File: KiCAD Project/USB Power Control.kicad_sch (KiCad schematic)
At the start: 24 parts, among them U5 TPS2561DRCR, U6 TPS2561DRCR, Y1 ECS-2520MV-240-BL-TR

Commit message: v1.0.0 RC2
Build candidate 2
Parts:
- U5, U6: Spec (none) -> TPS2561DRCR
- Y1: Spec (none) -> ECS-2520MV-240-BL-TR
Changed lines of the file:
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@@
 			)
 		)
+		(property "Spec" "TPS2561DRCR"
+			(at 96.52 27.94 0)
+			(effects
+				(font
+					(size 1.27 1.27)
+				)
+			)
+		)
 		(pin "10"
 		)
@@
 			)
 		)
+		(property "Spec" "TPS2561DRCR"
+			(at 96.52 91.44 0)
+			(effects
+				(font
+					(size 1.27 1.27)
+				)
+			)
+		)
 		(pin "10"
 		)
@@
 			)
 		)
+		(property "Spec" "ECS-2520MV-240-BL-TR"
+			(at 96.52 154.94 0)
+			(effects
+				(font
+					(size 1.27 1.27)
+				)
+			)
+		)

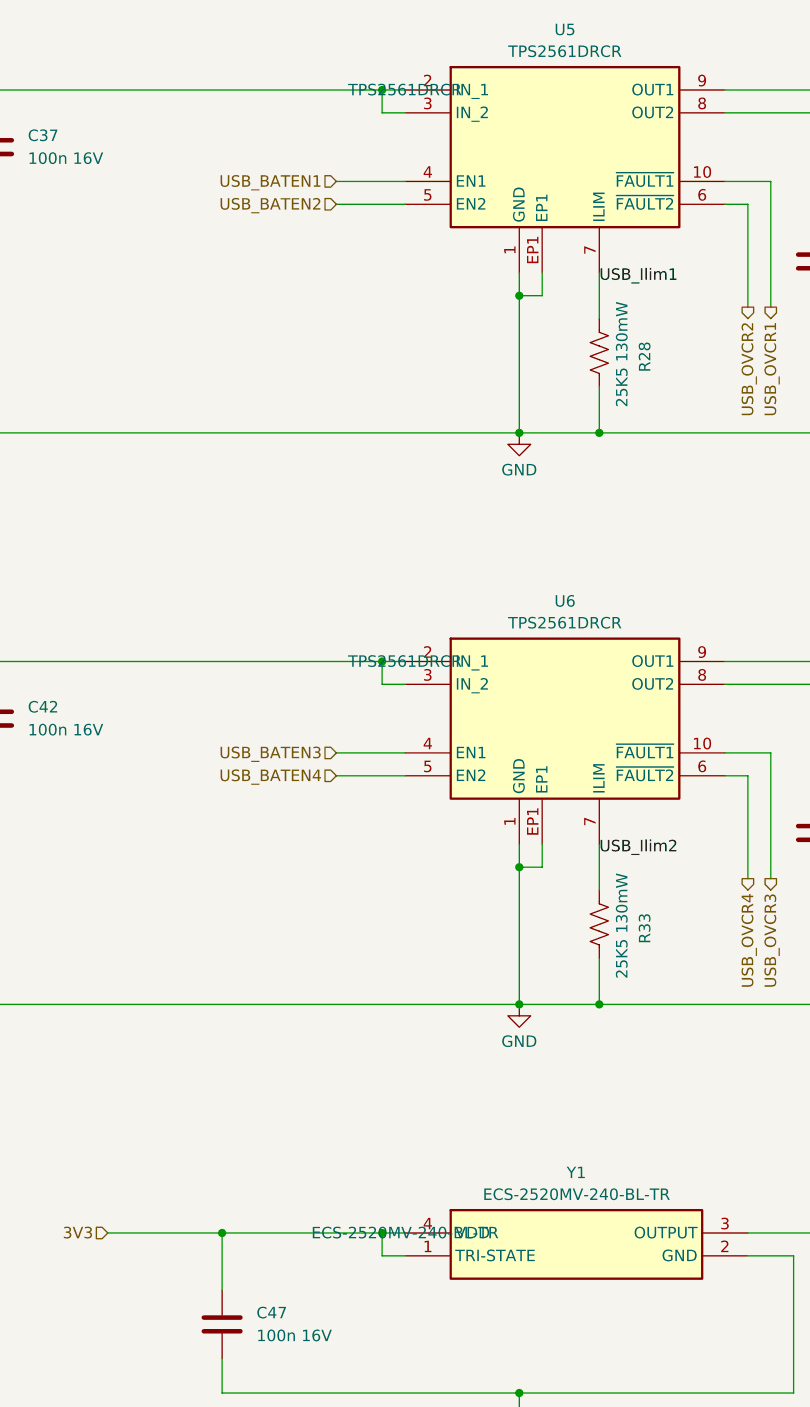
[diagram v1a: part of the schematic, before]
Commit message: v1.0.0 RC3
Minor change to upstream USB port to connect Vbus to ESD protection vice on-board 5V.
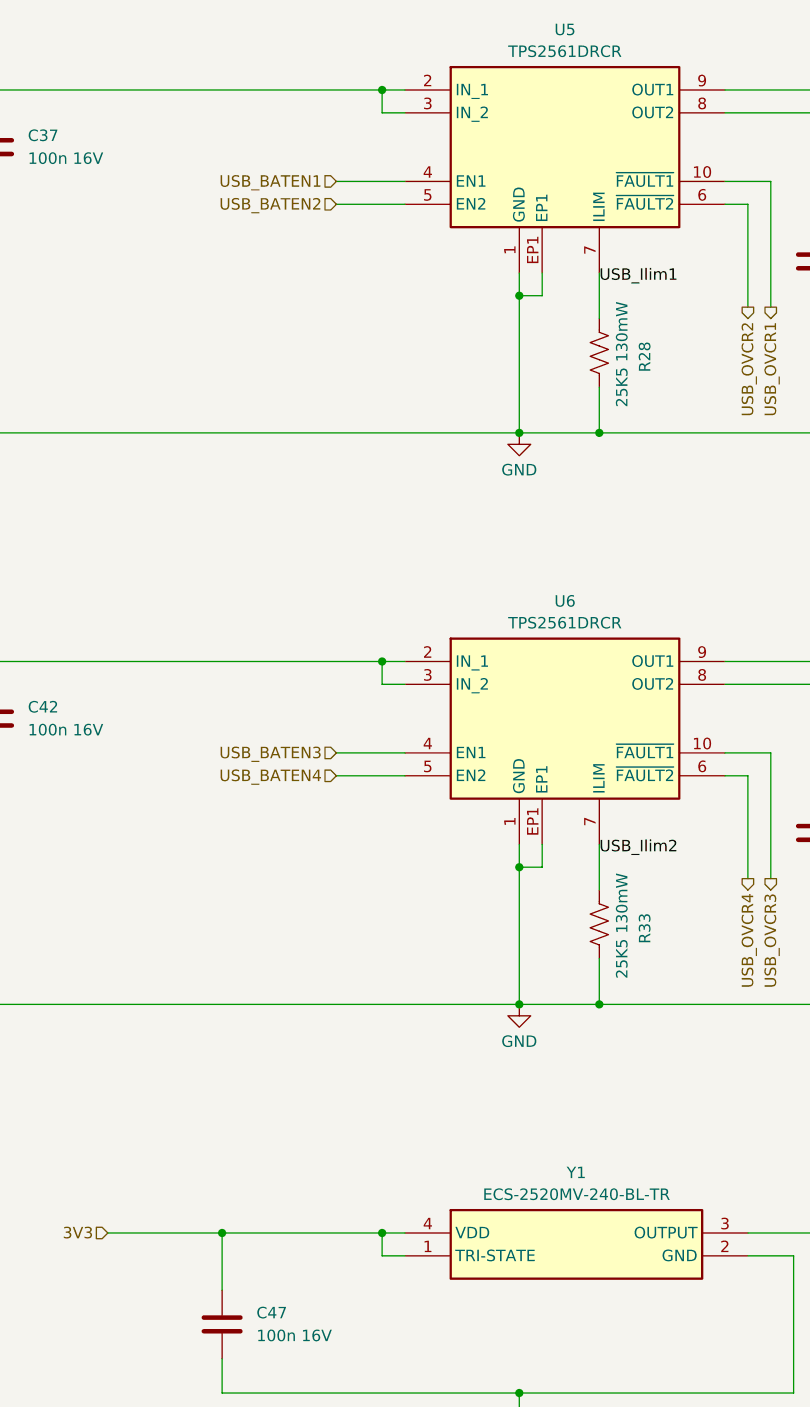
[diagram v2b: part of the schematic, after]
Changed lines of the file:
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@@
 		(title "1026 RPi Power Hat")
 		(date "2025-04-11")
-		(rev "1")
+		(rev "1.0.0 RC3")
 		(company "Dan Wilson")
 		(comment 1 "Copyright © 2025 Dan Wilson")
@@
 					(size 1.27 1.27)
 				)
+				(hide yes)
 			)
 		)
@@
 					(size 1.27 1.27)
 				)
+				(hide yes)
 			)
 		)
@@
 					(size 1.27 1.27)
 				)
+				(hide yes)
 			)
 		)

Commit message: v1.0.0A
Moved all symbols, footprints, and 3D models to local project-specific libraries in /KiCAD Project/Libraries.
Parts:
- C37, C38, C39, C42, C43, C45, C47, C48, C49, C50, C51: footprint Capacitor_SMD:C_0402_1005Metric -> 1026-3D:C_0402_1005Metric; symbol Device:C -> 1026-3D:C
- C40, C41, C44, C46: footprint DW_Passives:[C] Kyocera AVC Tant Poly TCJB157M006R0070 -> 1026-3D:[C] Kyocera AVC Tant Poly TCJB157M006R0070; symbol DW_Passives:[C] Kyocera AVX Tant Poly TCJB157M006R0070 -> 1026-3D:[C] Kyocera AVX Tant Poly TCJB157M006R0070
- FB3, FB4, FB5, FB6: footprint DW_Passives:[FB] Murata BLM18KG221SN1D 220ohm 2.2A -> 1026-3D:[FB] Murata BLM18KG221SN1D 220ohm 2.2A; symbol DW_Passives:[FB] Murata BLM18KG221SN1D 220ohm 2.2A -> 1026-3D:[FB] Murata BLM18KG221SN1D 220ohm 2.2A
- R28, R33: footprint Resistor_SMD:R_0402_1005Metric -> 1026-3D:R_0402_1005Metric; symbol Device:R_US -> 1026-3D:R_US
- U5, U6: footprint DW_Semiconductors:[U] TI USB Power Ctlr TPS2561DRCR -> 1026-3D:[U] TI USB Power Ctlr TPS2561DRCR; symbol DW_Semiconductors:[U] TI USB Power Ctlr TPS2561DRCR -> 1026-3D:[U] TI USB Power Ctlr TPS2561DRCR_1
- Y1: footprint DW_Semiconductors:[Y] ECS Clock Osc 24MHz ECS2520MV240BLTR -> 1026-3D:[Y] ECS Clock Osc 24MHz ECS2520MV240BLTR; symbol DW_Semiconductors:[Y] ECS Clock Osc 24Mhz ECS-2520MV-240-BL-TR -> 1026-3D:[Y] ECS Clock Osc 24Mhz ECS-2520MV-240-BL-TR
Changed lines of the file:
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@@
 	(symbol
 		(lib_name "[U] TI USB Power Ctlr TPS2561DRCR_1")
-		(lib_id "DW_Semiconductors:[U] TI USB Power Ctlr TPS2561DRCR")
+		(lib_id "1026-3D:[U] TI USB Power Ctlr TPS2561DRCR_1")
 		(at 96.52 27.94 0)
 		(unit 1)
@@
 			)
 		)
-		(property "Footprint" "DW_Semiconductors:[U] TI USB Power Ctlr TPS2561DRCR"
+		(property "Footprint" "1026-3D:[U] TI USB Power Ctlr TPS2561DRCR"
 			(at 128.27 122.86 0)
 			(effects
@@
 	)
 	(symbol
-		(lib_id "power:PWR_FLAG")
+		(lib_id "1026-3D:PWR_FLAG")
 		(at 222.25 91.44 0)
 		(unit 1)
@@
 	)
 	(symbol
-		(lib_id "Device:C")
+		(lib_id "1026-3D:C")
 		(at 50.8 34.29 180)
 		(unit 1)
@@
 			)
 		)
-		(property "Footprint" "Capacitor_SMD:C_0402_1005Metric"
+		(property "Footprint" "1026-3D:C_0402_1005Metric"
 			(at 49.8348 30.48 0)
 			(effects
@@
 	)
 	(symbol
-		(lib_id "Device:C")
+		(lib_id "1026-3D:C")
 		(at 167.64 110.49 180)
 		(unit 1)
@@
 			)
 		)
-		(property "Footprint" "Capacitor_SMD:C_0402_1005Metric"
+		(property "Footprint" "1026-3D:C_0402_1005Metric"
 			(at 166.6748 106.68 0)
 			(effects
@@
 	)
 	(symbol
-		(lib_id "power:GND")
+		(lib_id "1026-3D:GND")
 		(at 109.22 129.54 0)
 		(unit 1)
@@
 	)
 	(symbol
-		(lib_id "power:PWR_FLAG")
+		(lib_id "1026-3D:PWR_FLAG")
 		(at 222.25 27.94 0)
 		(unit 1)
@@
 	)
 	(symbol
-		(lib_id "Device:C")
+		(lib_id "1026-3D:C")
 		(at 142.24 110.49 180)
 		(unit 1)
@@
 			)
 		)
-		(property "Footprint" "Capacitor_SMD:C_0402_1005Metric"
+		(property "Footprint" "1026-3D:C_0402_1005Metric"
 			(at 141.2748 106.68 0)
 			(effects
@@
 	)
 	(symbol
-		(lib_id "DW_Passives:[C] Kyocera AVX Tant Poly TCJB157M006R0070")
+		(lib_id "1026-3D:[C] Kyocera AVX Tant Poly TCJB157M006R0070")
 		(at 179.07 40.64 270)
 		(unit 1)
@@
 			)
 		)
-		(property "Footprint" "DW_Passives:[C] Kyocera AVC Tant Poly TCJB157M006R0070"
+		(property "Footprint" "1026-3D:[C] Kyocera AVC Tant Poly TCJB157M006R0070"
 			(at 82.88 49.53 0)
 			(effects
@@
 	)
 	(symbol
-		(lib_id "Device:R_US")
+		(lib_id "1026-3D:R_US")
 		(at 118.11 57.15 0)
 		(unit 1)
@@
 			)
 		)
-		(property "Footprint" "Resistor_SMD:R_0402_1005Metric"
+		(property "Footprint" "1026-3D:R_0402_1005Metric"
 			(at 119.126 57.404 90)
 			(effects
@@
 	)
 	(symbol
-		(lib_id "DW_Passives:[FB] Murata BLM18KG221SN1D 220ohm 2.2A")
+		(lib_id "1026-3D:[FB] Murata BLM18KG221SN1D 220ohm 2.2A")
 		(at 195.58 93.98 0)
 		(mirror x)
@@
 			)
 		)
-		(property "Footprint" "DW_Passives:[FB] Murata BLM18KG221SN1D 220ohm 2.2A"
+		(property "Footprint" "1026-3D:[FB] Murata BLM18KG221SN1D 220ohm 2.2A"
 			(at 212.09 -0.94 0)
 			(effects
@@
 	)
 	(symbol
-		(lib_id "Device:C")
+		(lib_id "1026-3D:C")
 		(at 228.6 46.99 180)
 		(unit 1)
@@
 			)
 		)
-		(property "Footprint" "Capacitor_SMD:C_0402_1005Metric"
+		(property "Footprint" "1026-3D:C_0402_1005Metric"
 			(at 227.6348 43.18 0)
 			(effects
@@
 	)
 	(symbol
-		(lib_id "DW_Passives:[FB] Murata BLM18KG221SN1D 220ohm 2.2A")
+		(lib_id "1026-3D:[FB] Murata BLM18KG221SN1D 220ohm 2.2A")
 		(at 195.58 30.48 0)
 		(mirror x)
@@
 			)
 		)
-		(property "Footprint" "DW_Passives:[FB] Murata BLM18KG221SN1D 220ohm 2.2A"
+		(property "Footprint" "1026-3D:[FB] Murata BLM18KG221SN1D 220ohm 2.2A"
 			(at 212.09 -64.44 0)
 			(effects
@@
 	)
 	(symbol
-		(lib_id "DW_Passives:[C] Kyocera AVX Tant Poly TCJB157M006R0070")
+		(lib_id "1026-3D:[C] Kyocera AVX Tant Poly TCJB157M006R0070")
 		(at 154.94 104.14 270)
 		(unit 1)
@@
 			)
 		)
-		(property "Footprint" "DW_Passives:[C] Kyocera AVC Tant Poly TCJB157M006R0070"
+		(property "Footprint" "1026-3D:[C] Kyocera AVC Tant Poly TCJB157M006R0070"
 			(at 58.75 113.03 0)
 			(effects
@@
 	)
 	(symbol
-		(lib_id "power:PWR_FLAG")
+		(lib_id "1026-3D:PWR_FLAG")
 		(at 222.25 93.98 180)
 		(unit 1)
@@
 	)
 	(symbol
-		(lib_id "power:GND")
+		(lib_id "1026-3D:GND")
 		(at 109.22 66.04 0)
 		(unit 1)
@@
 	)
 	(symbol
-		(lib_id "DW_Passives:[FB] Murata BLM18KG221SN1D 220ohm 2.2A")
+		(lib_id "1026-3D:[FB] Murata BLM18KG221SN1D 220ohm 2.2A")
 		(at 195.58 27.94 0)
 		(unit 1)
@@
 			)
 		)
-		(property "Footprint" "DW_Passives:[FB] Murata BLM18KG221SN1D 220ohm 2.2A"
+		(property "Footprint" "1026-3D:[FB] Murata BLM18KG221SN1D 220ohm 2.2A"
 			(at 212.09 122.86 0)
 			(effects
@@
 	)
 	(symbol
-		(lib_id "Device:C")
+		(lib_id "1026-3D:C")
 		(at 167.64 46.99 180)
 		(unit 1)
@@
 			)
 		)
-		(property "Footprint" "Capacitor_SMD:C_0402_1005Metric"
+		(property "Footprint" "1026-3D:C_0402_1005Metric"
 			(at 166.6748 43.18 0)
 			(effects
@@
 	)
 	(symbol
-		(lib_id "Device:C")
+		(lib_id "1026-3D:C")
 		(at 215.9 110.49 180)
 		(unit 1)
@@
 			)
 		)
-		(property "Footprint" "Capacitor_SMD:C_0402_1005Metric"
+		(property "Footprint" "1026-3D:C_0402_1005Metric"
 			(at 214.9348 106.68 0)
 			(effects
@@
 	)
 	(symbol
-		(lib_id "Device:C")
+		(lib_id "1026-3D:C")
 		(at 228.6 110.49 180)
 		(unit 1)
@@
 			)
 		)
-		(property "Footprint" "Capacitor_SMD:C_0402_1005Metric"
+		(property "Footprint" "1026-3D:C_0402_1005Metric"
 			(at 227.6348 106.68 0)
 			(effects
@@
 	)
 	(symbol
-		(lib_id "Device:C")
+		(lib_id "1026-3D:C")
 		(at 50.8 97.79 180)
 		(unit 1)
@@
 			)
 		)
-		(property "Footprint" "Capacitor_SMD:C_0402_1005Metric"
+		(property "Footprint" "1026-3D:C_0402_1005Metric"
 			(at 49.8348 93.98 0)
 			(effects
@@
 	)
 	(symbol
-		(lib_id "Device:C")
+		(lib_id "1026-3D:C")
 		(at 142.24 46.99 180)
 		(unit 1)
@@
 			)
 		)
-		(property "Footprint" "Capacitor_SMD:C_0402_1005Metric"
+		(property "Footprint" "1026-3D:C_0402_1005Metric"
 			(at 141.2748 43.18 0)
 			(effects
@@
 	)
 	(symbol
-		(lib_id "power:PWR_FLAG")
+		(lib_id "1026-3D:PWR_FLAG")
 		(at 222.25 30.48 180)
 		(unit 1)
@@
 	(symbol
 		(lib_name "[U] TI USB Power Ctlr TPS2561DRCR_1")
-		(lib_id "DW_Semiconductors:[U] TI USB Power Ctlr TPS2561DRCR")
+		(lib_id "1026-3D:[U] TI USB Power Ctlr TPS2561DRCR_1")
 		(at 96.52 91.44 0)
 		(unit 1)
@@
 			)
 		)
-		(property "Footprint" "DW_Semiconductors:[U] TI USB Power Ctlr TPS2561DRCR"
+		(property "Footprint" "1026-3D:[U] TI USB Power Ctlr TPS2561DRCR"
 			(at 128.27 186.36 0)
 			(effects
@@
 	)
 	(symbol
-		(lib_id "DW_Passives:[C] Kyocera AVX Tant Poly TCJB157M006R0070")
+		(lib_id "1026-3D:[C] Kyocera AVX Tant Poly TCJB157M006R0070")
 		(at 154.94 40.64 270)
 		(unit 1)
@@
 			)
 		)
-		(property "Footprint" "DW_Passives:[C] Kyocera AVC Tant Poly TCJB157M006R0070"
+		(property "Footprint" "1026-3D:[C] Kyocera AVC Tant Poly TCJB157M006R0070"
 			(at 58.75 49.53 0)
 			(effects
@@
 	)
 	(symbol
-		(lib_id "power:GND")
+		(lib_id "1026-3D:GND")
 		(at 109.22 177.8 0)
 		(unit 1)
@@
 	)
 	(symbol
-		(lib_id "DW_Passives:[C] Kyocera AVX Tant Poly TCJB157M006R0070")
+		(lib_id "1026-3D:[C] Kyocera AVX Tant Poly TCJB157M006R0070")
 		(at 179.07 104.14 270)
 		(unit 1)
@@
 			)
 		)
-		(property "Footprint" "DW_Passives:[C] Kyocera AVC Tant Poly TCJB157M006R0070"
+		(property "Footprint" "1026-3D:[C] Kyocera AVC Tant Poly TCJB157M006R0070"
 			(at 82.88 113.03 0)
 			(effects
@@
 	)
 	(symbol
-		(lib_id "Device:R_US")
+		(lib_id "1026-3D:R_US")
 		(at 118.11 120.65 0)
 		(unit 1)
@@
 			)
 		)
-		(property "Footprint" "Resistor_SMD:R_0402_1005Metric"
+		(property "Footprint" "1026-3D:R_0402_1005Metric"
 			(at 119.126 120.904 90)
 			(effects
@@
 	)
 	(symbol
-		(lib_id "Device:C")
+		(lib_id "1026-3D:C")
 		(at 76.2 165.1 180)
 		(unit 1)
@@
 			)
 		)
-		(property "Footprint" "Capacitor_SMD:C_0402_1005Metric"
+		(property "Footprint" "1026-3D:C_0402_1005Metric"
 			(at 75.2348 161.29 0)
 			(effects
@@
 	)
 	(symbol
-		(lib_id "DW_Semiconductors:[Y] ECS Clock Osc 24Mhz ECS-2520MV-240-BL-TR")
+		(lib_id "1026-3D:[Y] ECS Clock Osc 24Mhz ECS-2520MV-240-BL-TR")
 		(at 96.52 154.94 0)
 		(unit 1)
@@
 			)
 		)
-		(property "Footprint" "DW_Semiconductors:[Y] ECS Clock Osc 24MHz ECS2520MV240BLTR"
+		(property "Footprint" "1026-3D:[Y] ECS Clock Osc 24MHz ECS2520MV240BLTR"
 			(at 130.81 249.86 0)
 			(effects
@@
 	)
 	(symbol
-		(lib_id "Device:C")
+		(lib_id "1026-3D:C")
 		(at 215.9 46.99 180)
 		(unit 1)
@@
 			)
 		)
-		(property "Footprint" "Capacitor_SMD:C_0402_1005Metric"
+		(property "Footprint" "1026-3D:C_0402_1005Metric"
 			(at 214.9348 43.18 0)
 			(effects
@@
 	)
 	(symbol
-		(lib_id "DW_Passives:[FB] Murata BLM18KG221SN1D 220ohm 2.2A")
+		(lib_id "1026-3D:[FB] Murata BLM18KG221SN1D 220ohm 2.2A")
 		(at 195.58 91.44 0)
 		(unit 1)
@@
 			)
 		)
-		(property "Footprint" "DW_Passives:[FB] Murata BLM18KG221SN1D 220ohm 2.2A"
+		(property "Footprint" "1026-3D:[FB] Murata BLM18KG221SN1D 220ohm 2.2A"
 			(at 212.09 186.36 0)
 			(effects
